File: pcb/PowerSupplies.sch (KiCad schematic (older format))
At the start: 20 parts, among them Q12 ZXTP25020DGTA, U13 TL431BQDBZR, U2 LM2937EM-5.0, U3 LM2937EM-5.0

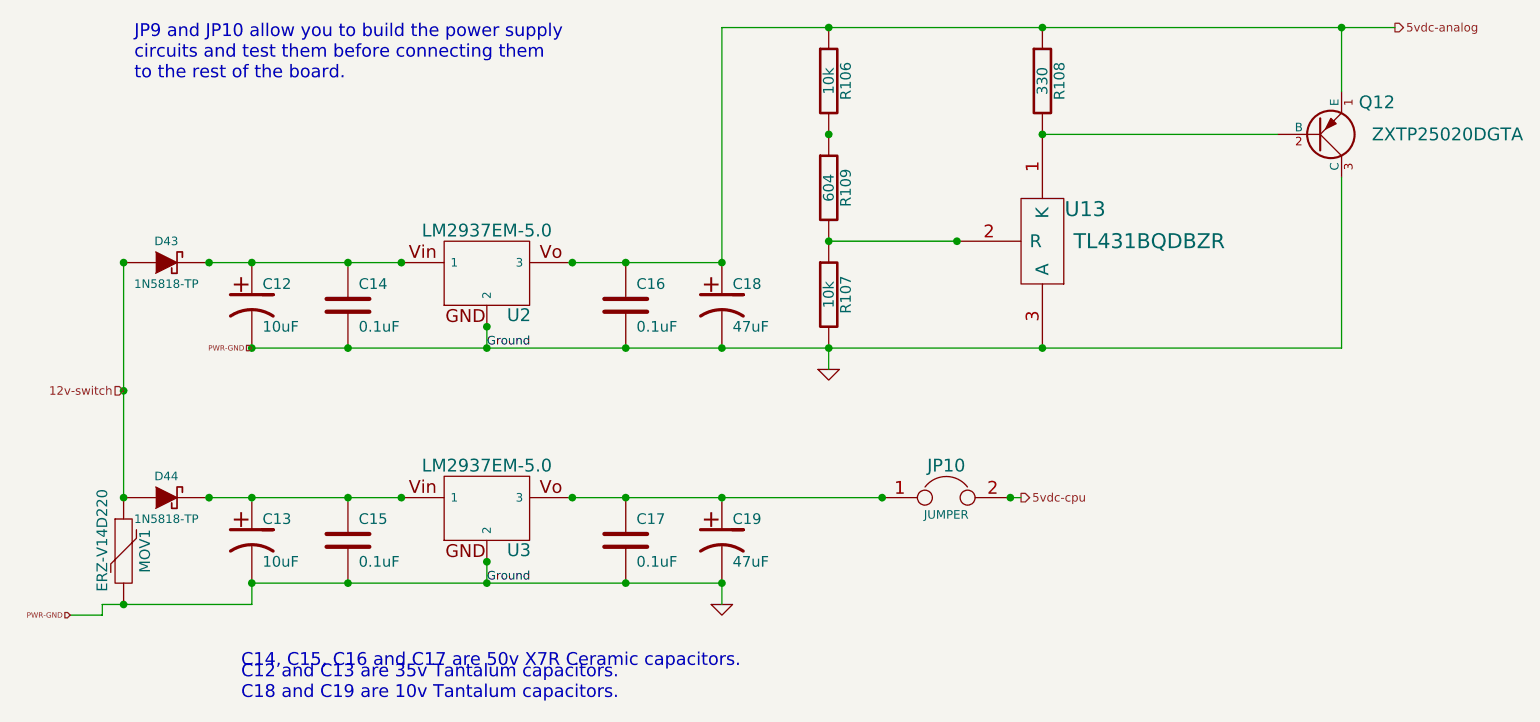
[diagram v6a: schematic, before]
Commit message: Added 5.6v zener diode to output of CPU 5v filtering capacitors to clamp voltage spikes.
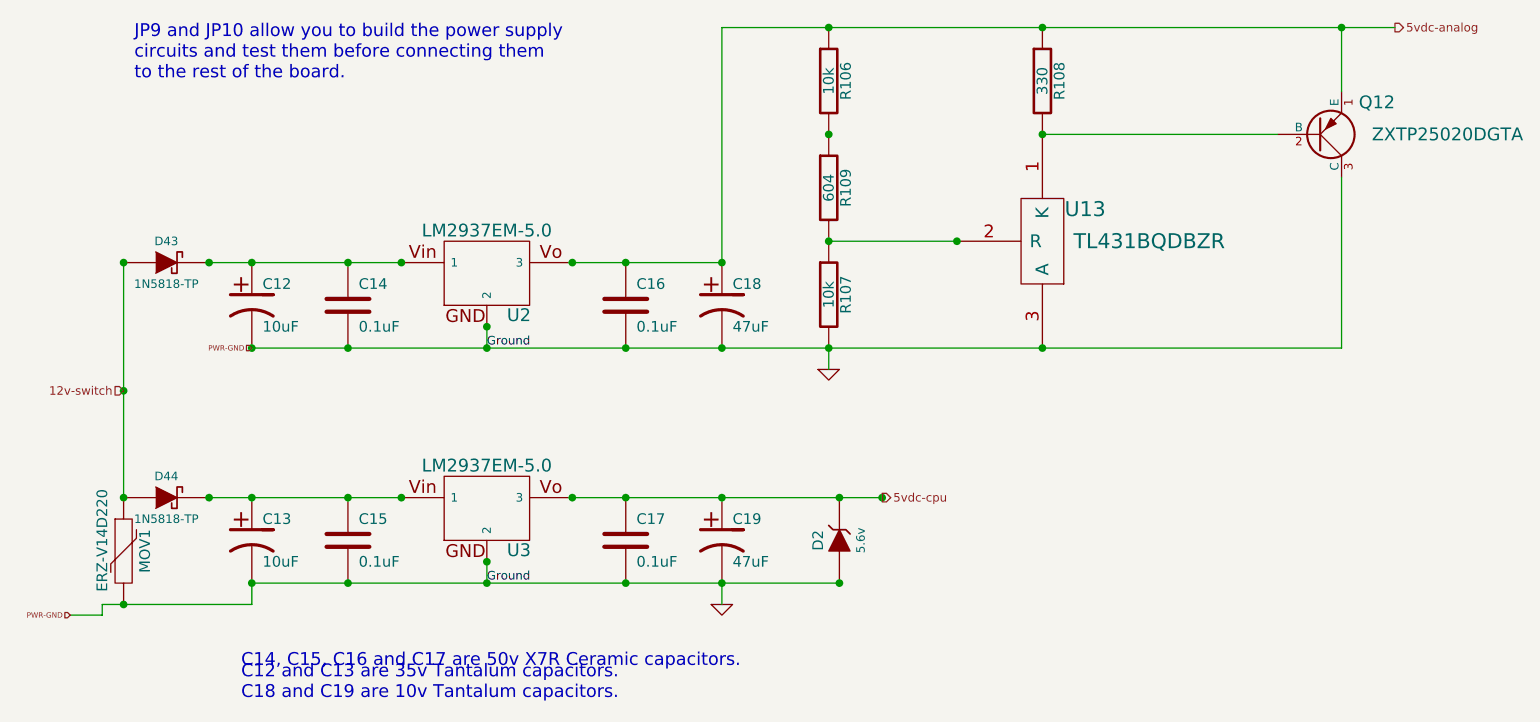
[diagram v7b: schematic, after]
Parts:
- removed JP10: JUMPER, symbol JUMPER
- added D2: 5.6v, symbol ZENER
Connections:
- net 5vdc-cpu: now also C17.1, C19.1 (+), U3.3, D2.2 (K)
- net GND: now also D2.1 (A)
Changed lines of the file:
@@
-EESchema Schematic File Version 2  date Tue 14 May 2013 05:29:01 PM EDT
+EESchema Schematic File Version 2  date Wed 15 May 2013 02:06:49 PM EDT
 LIBS:opto
 LIBS:power
@@
 Sheet 7 7
 Title "Jaguar PCB for FreeEMS"
-Date "14 may 2013"
+Date "15 may 2013"
 Rev "0.6-alpha"
 Comp "git hash: xxxxxxxxxx"
@@
 Comment4 ""
 $EndDescr
+Connection ~ 5100 3750
+Connection ~ 5100 3350
+Wire Wire Line
+	5100 3750 2350 3750
+Wire Wire Line
+	7450 1850 7450 2650
+Wire Wire Line
+	7700 1150 4550 1150
+Connection ~ 6050 1150
+Connection ~ 5050 1150
+Wire Wire Line
+	4550 1150 4550 2250
+Wire Wire Line
+	4550 2250 3850 2250
+Connection ~ 1750 2250
+Connection ~ 2150 2250
+Wire Wire Line
+	3050 2250 2150 2250
+Wire Wire Line
+	4550 3750 4550 3850
+Wire Wire Line
+	2350 3750 2350 3850
+Wire Wire Line
+	3850 3350 5300 3350
+Connection ~ 1750 3350
+Connection ~ 1750 3850
+Connection ~ 3450 2650
+Wire Wire Line
+	3450 2650 3450 2550
+Connection ~ 4550 3750
+Connection ~ 4550 3350
+Connection ~ 4100 3750
+Connection ~ 4100 3350
+Connection ~ 3850 3350
+Connection ~ 3450 3650
+Connection ~ 2350 3750
+Connection ~ 2800 3750
+Connection ~ 3050 3350
+Connection ~ 2800 3350
+Connection ~ 2350 3350
+Connection ~ 2350 2650
+Connection ~ 2800 2650
+Connection ~ 3450 2550
+Connection ~ 4100 2650
+Connection ~ 4550 2650
+Connection ~ 4550 2250
+Connection ~ 4100 2250
+Connection ~ 3850 2250
+Connection ~ 3050 2250
+Connection ~ 2800 2250
+Connection ~ 2350 2250
+Wire Wire Line
+	3450 3750 3450 3650
+Connection ~ 3450 3750
+Wire Wire Line
+	5050 2650 5050 2750
+Wire Wire Line
+	1750 2250 1750 3350
+Connection ~ 1750 2850
+Connection ~ 5300 3350
+Wire Wire Line
+	1500 3900 1650 3900
+Wire Wire Line
+	1650 3900 1650 3850
+Wire Wire Line
+	1650 3850 2350 3850
+Wire Wire Line
+	3050 3350 2150 3350
+Connection ~ 2150 3350
+Connection ~ 5050 2650
+Wire Wire Line
+	5650 2150 5050 2150
+Wire Wire Line
+	7150 1650 6050 1650
+Wire Wire Line
+	7450 2650 2350 2650
+Connection ~ 6050 2650
+Connection ~ 6050 1650
+Connection ~ 5650 2150
+Connection ~ 5050 2150
+Connection ~ 5050 1650
+Wire Wire Line
+	7450 1450 7450 1150
 Connection ~ 7450 1150
-Wire Wire Line
-	7450 1450 7450 1150
-Connection ~ 5050 1650
-Connection ~ 5050 2150
-Connection ~ 5650 2150
-Connection ~ 6050 1650
-Connection ~ 6050 2650
-Wire Wire Line
-	2350 2650 7450 2650
-Wire Wire Line
-	7150 1650 6050 1650
-Wire Wire Line
-	5650 2150 5050 2150
-Connection ~ 5050 2650
-Connection ~ 2150 3350
-Wire Wire Line
-	3050 3350 2150 3350
-Wire Wire Line
-	1650 3850 2350 3850
-Wire Wire Line
-	1650 3850 1650 3900
-Wire Wire Line
-	1650 3900 1500 3900
-Connection ~ 5300 3350
-Connection ~ 5900 3350
-Wire Wire Line
-	5900 3350 5950 3350
-Connection ~ 1750 2850
-Wire Wire Line
-	1750 2250 1750 3350
-Wire Wire Line
-	5050 2650 5050 2750
-Wire Wire Line
-	2350 3750 4550 3750
-Connection ~ 3450 3750
-Wire Wire Line
-	3450 3750 3450 3650
-Connection ~ 2350 2250
-Connection ~ 2800 2250
-Connection ~ 3050 2250
-Connection ~ 3850 2250
-Connection ~ 4100 2250
-Connection ~ 4550 2250
-Connection ~ 4550 2650
-Connection ~ 4100 2650
-Connection ~ 3450 2550
-Connection ~ 2800 2650
-Connection ~ 2350 2650
-Connection ~ 2350 3350
-Connection ~ 2800 3350
-Connection ~ 3050 3350
-Connection ~ 2800 3750
-Connection ~ 2350 3750
-Connection ~ 3450 3650
-Connection ~ 3850 3350
-Connection ~ 4100 3350
-Connection ~ 4100 3750
-Connection ~ 4550 3350
-Connection ~ 4550 3750
-Wire Wire Line
-	3450 2650 3450 2550
-Connection ~ 3450 2650
-Connection ~ 1750 3850
-Connection ~ 1750 3350
-Wire Wire Line
-	3850 3350 5300 3350
-Wire Wire Line
-	2350 3750 2350 3850
-Wire Wire Line
-	4550 3750 4550 3850
-Wire Wire Line
-	3050 2250 2150 2250
-Connection ~ 2150 2250
-Connection ~ 1750 2250
-Wire Wire Line
-	3850 2250 4550 2250
-Wire Wire Line
-	4550 2250 4550 1150
-Connection ~ 5050 1150
-Connection ~ 6050 1150
-Wire Wire Line
-	4550 1150 7700 1150
-Wire Wire Line
-	7450 2650 7450 1850
+$Comp
+L ZENER D2
+U 1 1 5193C4AB
+P 5100 3550
+F 0 "D2" H 5100 3650 50  0000 C CNN
+F 1 "5.6v" H 5100 3450 40  0000 C CNN
+	1    5100 3550
+	0    -1   -1   0
+$EndComp
 $Comp
 L PNP Q12
@@
 JP9 and JP10 allow you to build the power supply\ncircuits and test them before connecting them\nto the rest of the board.
 $Comp
-L JUMPER JP10
-U 1 1 4F401512
-P 5600 3350
-F 0 "JP10" H 5600 3500 60  0000 C CNN
-F 1 "JUMPER" H 5600 3270 40  0000 C CNN
-	1    5600 3350
-	1    0    0    -1
-$EndComp
-$Comp
 L VR MOV1
 U 1 1 4F24F92A
@@
 Text HLabel 7700 1150 2    40   Output ~ 0
 5vdc-analog
-Text HLabel 5950 3350 2    40   Output ~ 0
+Text HLabel 5300 3350 2    40   Output ~ 0
 5vdc-cpu
 $Comp
